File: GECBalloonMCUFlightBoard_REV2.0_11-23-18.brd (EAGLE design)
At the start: 160 x 100 mm, 67 parts, among them IC1 PIC32MX360F512L, U1 ADS1118, U2 ADS1118, X2 MALE_VGA, Y1 SG-636PCW_50.0000MC3__ROHS

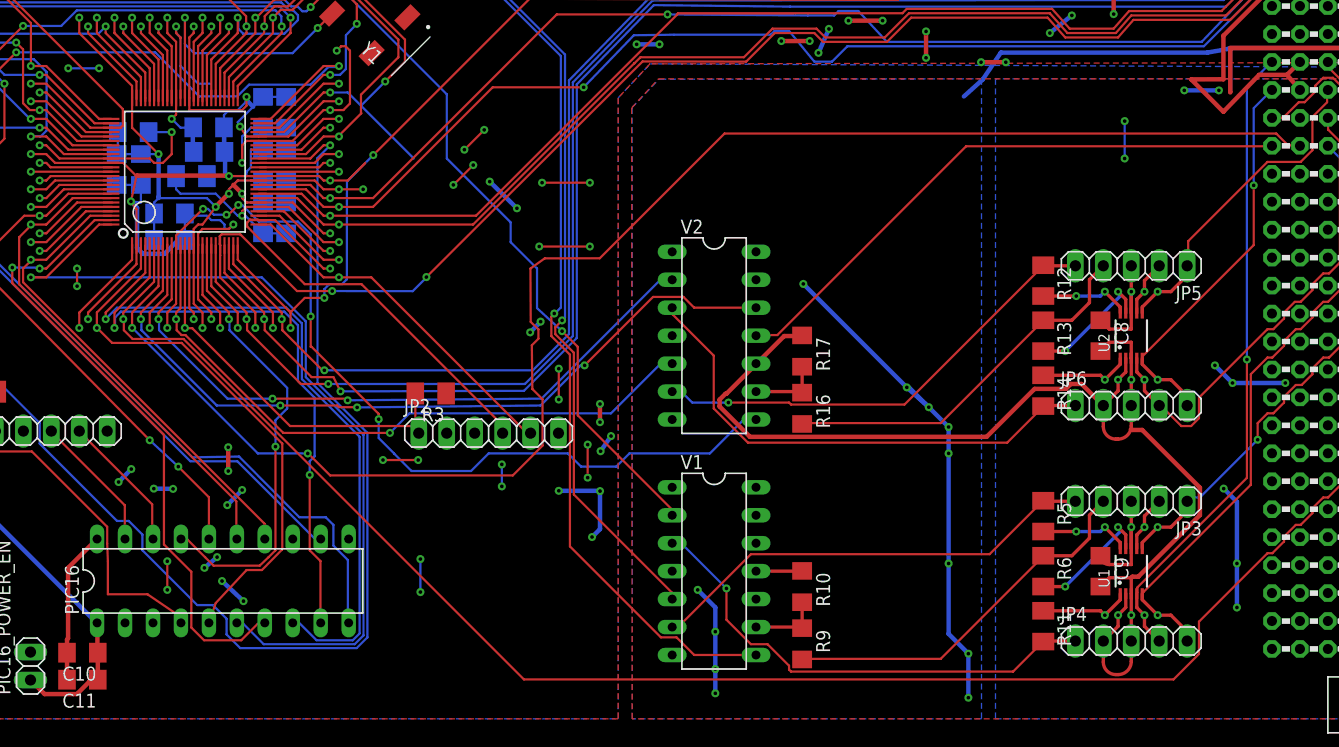
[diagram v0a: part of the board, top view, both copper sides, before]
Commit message: Swapped out oscillator for external crystal clock and connected GND and 3V3 planes better.
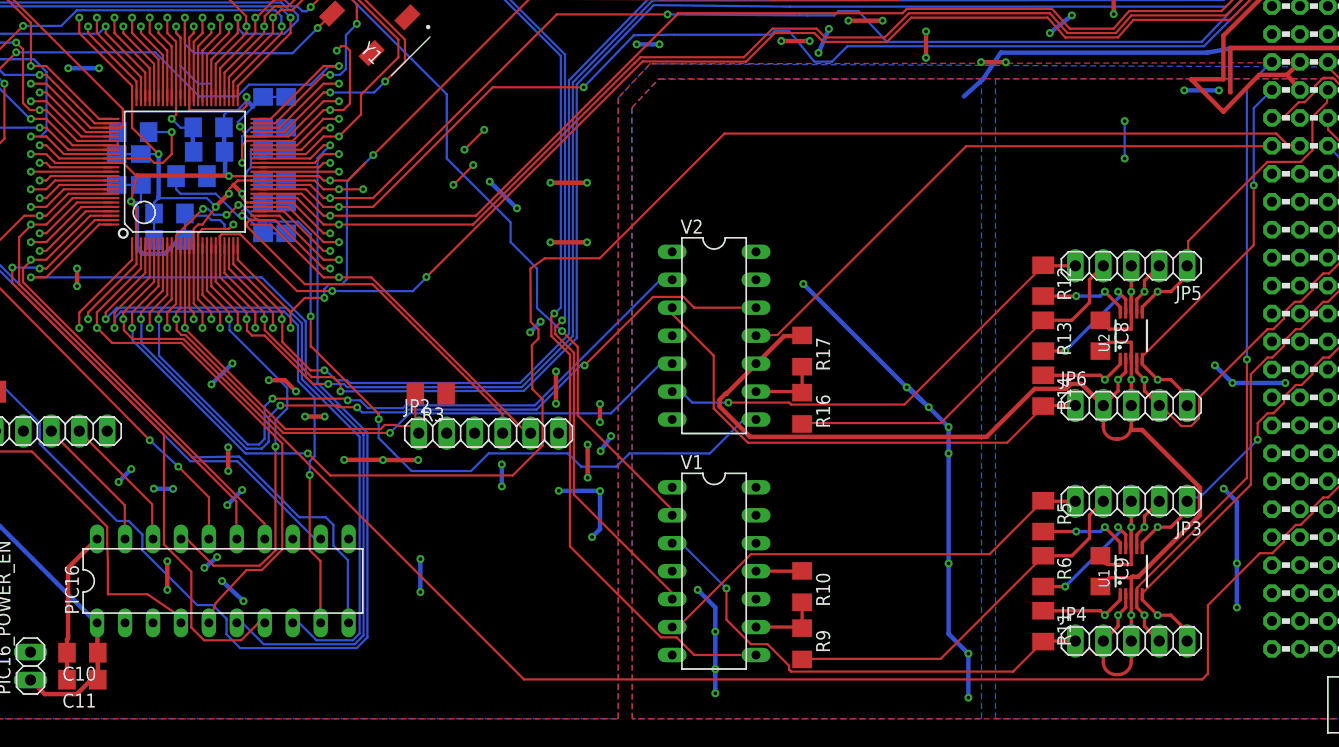
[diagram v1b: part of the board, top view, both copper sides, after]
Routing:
- net GPSPPS: track 148.8 -> 141.1 mm
- net SCK2: track 62.0 -> 69.2 mm
- net GND_3V3: track 190.9 -> 196.9 mm, vias 52 -> 57
- net PIC_COND_EN: track 71.8 -> 77.5 mm
- net +3V3: track 176.2 -> 178.9 mm, vias 51 -> 53
- net CHARGE_PROBE_0: track 174.2 -> 176.1 mm
- net TEMP_2: track 142.3 -> 144.1 mm
- net CHARGE_PROBE_1: track 144.9 -> 145.6 mm
- net PGED2: track 41.3 -> 41.9 mm
